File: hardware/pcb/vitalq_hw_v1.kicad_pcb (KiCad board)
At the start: 4 copper layers, 36.5 x 70 mm, 245 parts, among them J1 USB-C, J2 LiPo pads, J3 FSR pads, J5 ECG pads, J6 EDA pads, J7 Chest bioZ, J8 TC2030, Q1 CSD13380F3T, Q2 CSD13380F3T, Q3 BC847BS,115, SW1 TS-1088, SW2 TS-1088, U1 ESP32-WROOM-32E-N8R2, U10 AS7341-DLGM, U11 TMP117AIDRVR, U12 MLX90632SLD-DCB-100-SP, U13 BME280, U14 LSM6DSV80XTR, U15 TPS61240YFFR, U16 SFH 7072, U17 MAX17048G+T10, U18 W25Q512JVEIQ, U19 TCA6408ARSVR, U2 BQ25170DSGR, U20 TMP117AIDRVR, U21 USBLC6-2SC6, U3 TPS63802DLAR, U4 TPS7A2018PDBVR, U5 CP2102N-A02-GQFN28R, U6 AFE4900YZR, U7 AD5940BCBZ-RL7, U8 ADS1292RIRSMT, U9 PCA9306DCUR

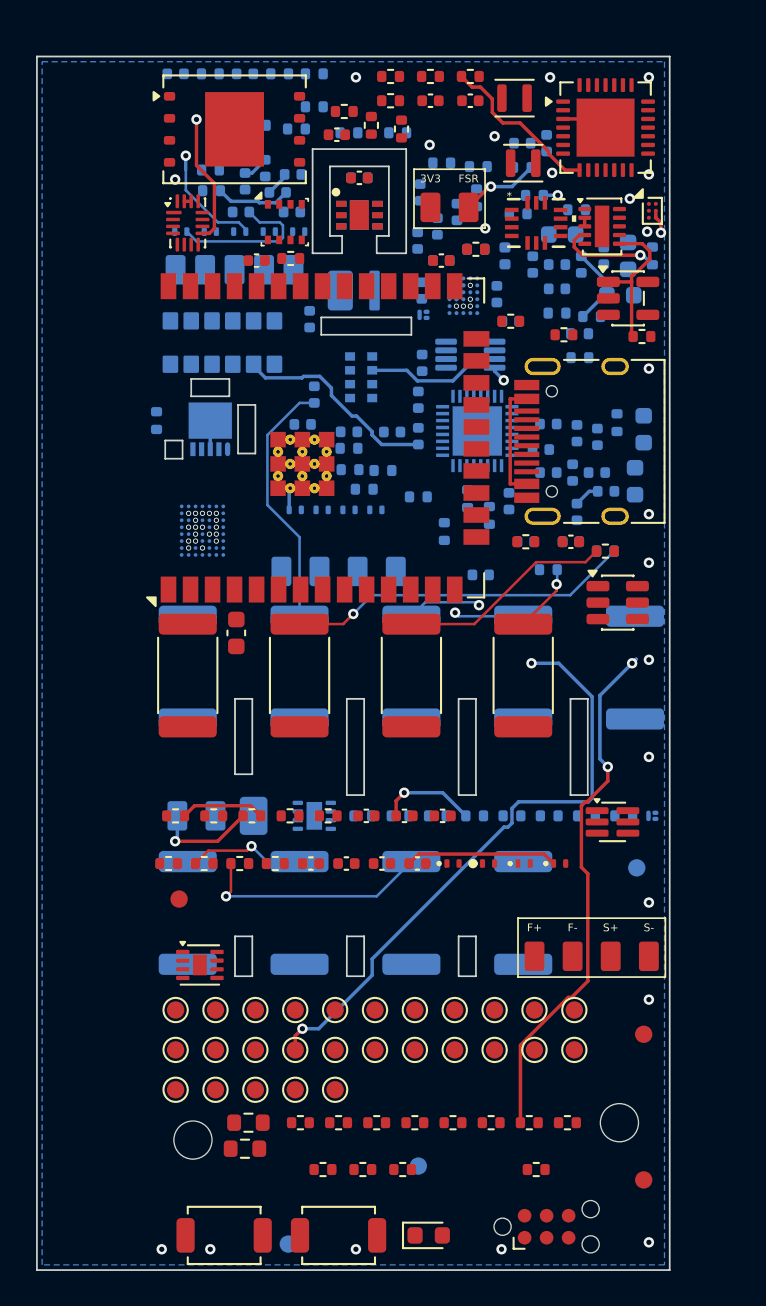
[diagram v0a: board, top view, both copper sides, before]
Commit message: Repack hw_v1 placement: skin-sensor cluster + per-IC passives, zero removals
Placement-only pass on the pcb branch — all 245 parts retained, none
removed, no footprints changed. Every skin-facing sensor stays in one
~16x16 mm bottom-side cluster around the same skin point (J5 ECG pads,
SFH7072, MLX90632, AS7341, D10+D11 LEDs, TMP117 pair). D11 (860 nm)
moved beside D10 so both emitters light the AS7341 aperture.

Per-IC support passives pulled tight: AFE4900 supply/ref network wraps
U7; ADS1292R input/RLD network hugs U8; AD5940 loop + isolated
electrode path (C54-C55, R39-R42, D6-D9) at U6 and along the J6
corridor; PCA9306 I2C pull-ups flank U9; USB-UART series resistors
moved beside the connector row.

check.sh: 0 clashes, 0 pad-to-slot/edge, 0 SMD-vs-PTH, 0 pad-miss.
Non-unconnected DRC errors 28 (vs 29 at the branch tip) — all
pre-existing (U1 pad-25 VIP vias, Q1/Q2 package proximity, J5 clamp
diodes inside the HV rule). Board remains intentionally unrouted.

Research prototype. Not a medical device.

Co-Authored-By: Devin AI <158243242+devin-ai-integration[bot]@users.noreply.github.com>
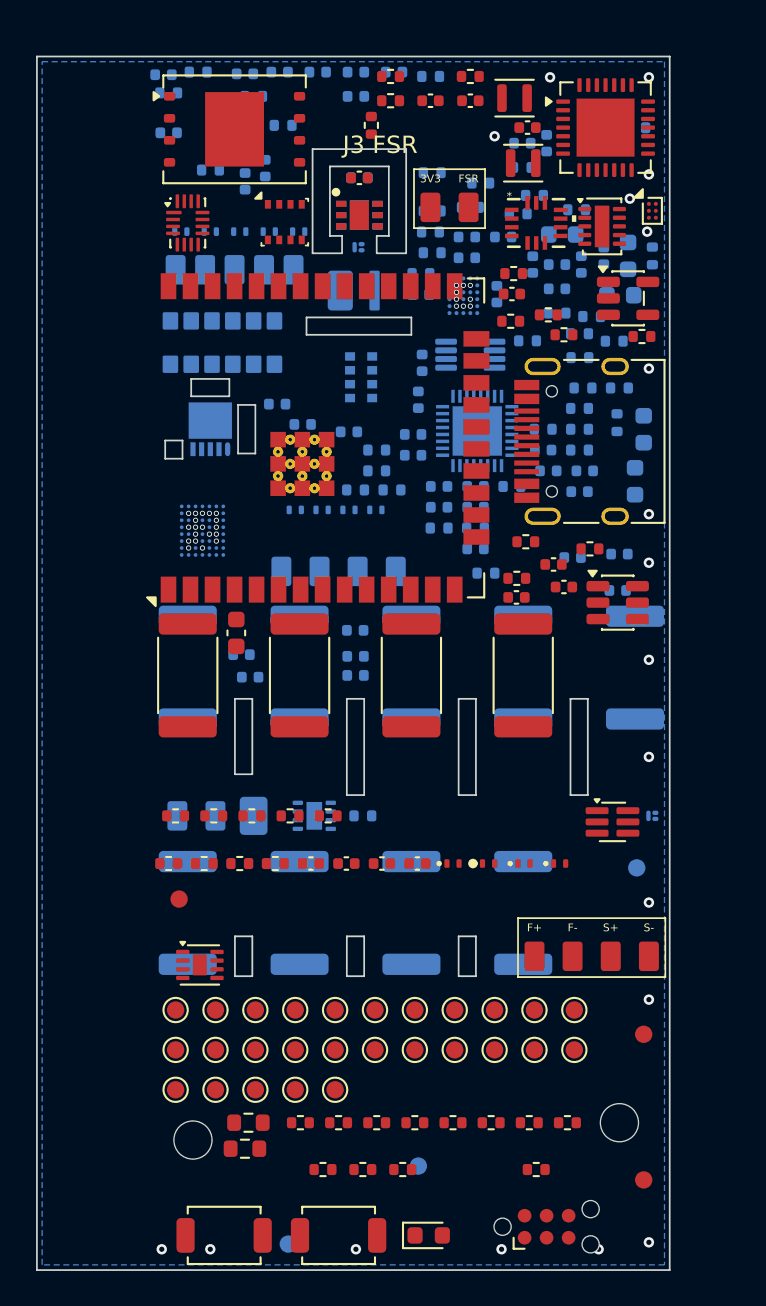
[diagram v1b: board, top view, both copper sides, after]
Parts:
- C54, C66, R53, R63: moved to B.Cu
- moved R71 41.0 mm to (32.5, 2.91)
- moved R70 40.0 mm to (32.5, 4.11)
- moved R73 39.7 mm to (34.6, 4.11)
- moved R72 38.5 mm to (32.5, 5.31)
- moved C30 32.4 mm to (25.3, 28.4)
- moved C16 31.9 mm to (7.30, 1.05)
- moved R12 30.6 mm to (7.60, 2.10), turned to 180 degrees
- moved C19 30.5 mm to (16.2, 0.90)
- moved C18 28.6 mm to (14.0, 0.90), turned to 180 degrees
- moved R18 28.1 mm to (31.5, 19.1)
- moved R30 27.9 mm to (25.9, 29.8)
- moved C24 27.6 mm to (7.60, 4.40)
- moved C26 27.1 mm to (20.6, 0.90)
- moved R13 26.3 mm to (12.5, 2.30), turned to 180 degrees
- moved C23 26.3 mm to (18.4, 0.90), turned to 180 degrees
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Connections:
- H1 pad : (no net) -> unconnected-(H1-MH-Pad1)
- H2 pad : (no net) -> unconnected-(H2-MH-Pad1)
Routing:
- net TX_5V_RAW: track 58.3 -> 0.00 mm, vias 3 -> 0
- net RLD_CLAMP: track 56.5 -> 0.00 mm, vias 3 -> 0
- net I2C_SDA_1V8: track 52.7 -> 0.00 mm, vias 3 -> 0
- net GND: track 43.9 -> 0.00 mm, vias 25 -> 26
- net AFE_P_AC: track 31.7 -> 0.00 mm, vias 3 -> 0
- net VBUS_DET: track 31.3 -> 0.00 mm, vias 2 -> 0
- net SE_SURGE: track 19.9 -> 0.00 mm, vias 1 -> 0
- net ECG_N: track 14.7 -> 0.00 mm
- net SP_SURGE: track 13.5 -> 0.00 mm, vias 1 -> 0
- net RE_SURGE: track 12.4 -> 0.00 mm
- net TX_5V: track 11.9 -> 0.00 mm
- net CP_VBUS: track 9.58 -> 0.00 mm
- net +3V3: track 9.10 -> 0.00 mm
- net ECG_P: track 8.83 -> 0.00 mm
- net SN_ISO: track 8.78 -> 0.00 mm
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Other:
- outline, holes or cut-outs redrawn
- board text added: "J3 FSR"

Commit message: Improve hw_v2 PCB: HV tail chains, decoupling re-park, power islands, U22 escape
Schematic fixes:
- Fix SWEAT_RE silently shorted to GND (D27 pin-endpoint collision)
- Fix L2/TX_5V boost miswire (VBAT_SYS->TX_SW, rail was dead)
- Add J11/J13 HV-boundary chains: R118-R122 2512 cut-points + D26-D30 DNP TPD clamps
- Correct J12 to FH12-14S-0.5SH land; R114 LED_AN fed from TX_5V
- Move U24 VBACKUP to dedicated RTC_VBK net; ADS1292 CLK grounded
- Add CS pull-ups (R115-R117), TP28, C84 (U4 +3V3 input decoupling)
- New hw_v2 parts: U22 MAX86178, U23 SHT45, U24 RTC (DNP), U25 IM69D130 (DNP),
  D12 SFH4735 NIR + Q4 gate, J9-J13 tails

Layout:
- Grow board 32->40 mm east; five 2512 HV parts could not fit at 32 mm
- Re-park ~30 decoupling passives adjacent to their ICs
- Replace phantom moat wall slots with a real >=1.0 mm channel
- Own-layer pour keepouts under HV pads; wider stitch-via HV margin
- U22 WLP: drop 28 NC lands (rows B-E) to open B.Cu escape for F-row
- Retarget dead power islands (TX_5V over its 9 loads, +1V8 under LDO, +3V3 at U7)

BOM/CPL: footprint-aware 0R mapping (0402->C17168, 2512->C2908946),
DNP parts excluded, J11/J13 pads DNP'd, U1 MPN corrected.

Gates: placement zero (291 parts), ERC 0, DRC non-unrouted 0
(9 inherent Q1/Q2/Q4 intra-package clearances waived-by-name).
Board remains unrouted by design - research prototype, not fab-ready.

Generated with [Devin](https://devin.ai)

Co-Authored-By: Devin <158243242+devin-ai-integration[bot]@users.noreply.github.com>
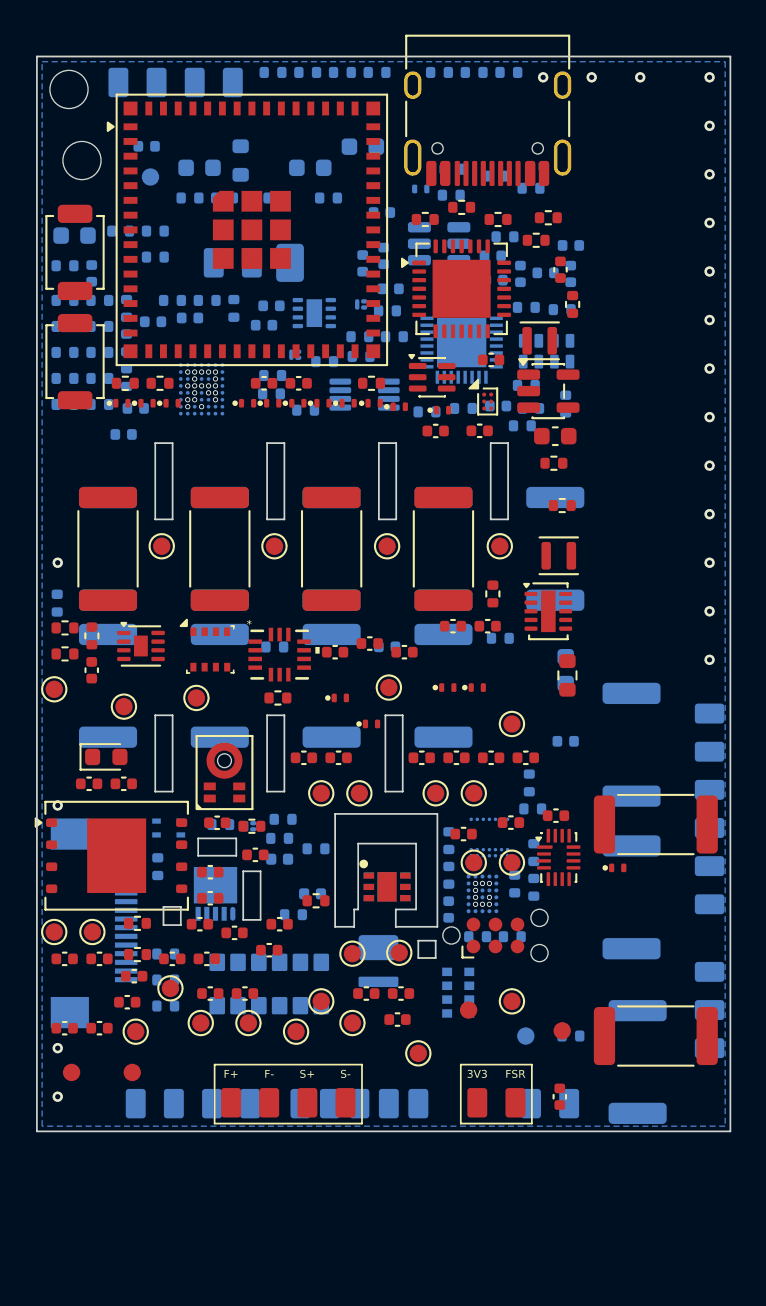
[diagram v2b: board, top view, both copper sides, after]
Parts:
- added C76: 100n, Capacitor_SMD:C_0402_1005Metric, F.Cu at (3.61, 56.0)
- added C77: 100n, Capacitor_SMD:C_0402_1005Metric, F.Cu at (19.0, 54.0)
- added C78: 100n, Capacitor_SMD:C_0402_1005Metric, F.Cu at (21.0, 54.0)
- added C79: 100n, Capacitor_SMD:C_0402_1005Metric, F.Cu at (20.8, 55.5)
- added C80: 1u, Capacitor_SMD:C_0402_1005Metric, B.Cu at (30.5, 39.5)
- added C81: 100n, Capacitor_SMD:C_0402_1005Metric, F.Cu at (30.2, 60.0)
- added C82: 1u, Capacitor_SMD:C_0402_1005Metric, F.Cu at (10.4, 44.2)
- added C83: 1u, Capacitor_SMD:C_0402_1005Metric, F.Cu at (24.6, 44.9)
- added C84: 1u, Capacitor_SMD:C_0402_1005Metric, B.Cu at (28.5, 20.3)
- added D12: SFH 4735 730nm, LED_SMD:LED_0402_1005Metric, B.Cu at (15.9, 48.3)
- added D26: TPD1E10B06, vitalq:TPD1E10B06_DPY, F.Cu at (17.5, 37.0)
- added D27: TPD1E10B06, vitalq:TPD1E10B06_DPY, F.Cu at (23.7, 36.4)
- added D28: TPD1E10B06, vitalq:TPD1E10B06_DPY, F.Cu at (25.4, 36.4)
- added D29: TPD1E10B06, vitalq:TPD1E10B06_DPY, F.Cu at (33.5, 46.8)
- added D30: TPD1E10B06, vitalq:TPD1E10B06_DPY, F.Cu at (19.3, 38.5)
- added J10: Optical tail pads, vitalq:Pads_1x06, B.Cu at (38.8, 43.4)
- added J11: Sweat site, vitalq:Pads_1x03, B.Cu at (38.8, 55.0)
- added J12: FH12-14S, Connector_FFC-FPC:Hirose_FH12-14S-0.5SH_1x14-1MP_P0.50mm_Horizontal, B.Cu at (3.30, 50.0)
- added J13: MX ECG pads, vitalq:Pads_1x02, B.Cu at (29.6, 60.4)
- added J9: I2C tail pads, vitalq:Pads_1x04, B.Cu at (8.00, 1.50)
- added Q4: CSD13380F3T, Package_DFN_QFN:Texas_PicoStar_DFN-3_0.69x0.60mm, B.Cu at (12.3, 44.4)
- added R102: 0, Resistor_SMD:R_0402_1005Metric, B.Cu at (23.9, 8.00)
- added R103: 0, Resistor_SMD:R_0402_1005Metric, B.Cu at (26.4, 6.90)
- added R104: 0, Resistor_SMD:R_0402_1005Metric, B.Cu at (28.5, 7.60)
- added R105: 0, Resistor_SMD:R_0402_1005Metric, B.Cu at (24.0, 6.50)
- added R106: 0, Resistor_SMD:R_0402_1005Metric, B.Cu at (8.83, 8.16)
- added R107: 100k, Resistor_SMD:R_0402_1005Metric, B.Cu at (10.8, 8.16)
- added R108: 100k, Resistor_SMD:R_0402_1005Metric, B.Cu at (12.8, 8.16)
- added R109: 100, Resistor_SMD:R_0402_1005Metric, F.Cu at (16.1, 48.7)
- added R110: 100k, Resistor_SMD:R_0402_1005Metric, B.Cu at (14.2, 44.0)
- added R112: 10k, Resistor_SMD:R_0402_1005Metric, B.Cu at (4.83, 10.1)
- added R113: 10k, Resistor_SMD:R_0402_1005Metric, B.Cu at (6.83, 10.1)
- added R114: 0, Resistor_SMD:R_0402_1005Metric, F.Cu at (12.4, 44.4)
- added R115: 10k, Resistor_SMD:R_0402_1005Metric, B.Cu at (28.0, 21.3)
- added R116: 10k, Resistor_SMD:R_0402_1005Metric, B.Cu at (30.8, 56.5)
- added R117: 10k, Resistor_SMD:R_0402_1005Metric, B.Cu at (28.4, 41.9)
- added R118: 0, Resistor_SMD:R_2512_6332Metric, F.Cu at (35.7, 44.3)
- added R119: 0, Resistor_SMD:R_2512_6332Metric, F.Cu at (35.7, 56.5)
- added R120: 0, Resistor_SMD:R_2512_6332Metric, B.Cu at (34.3, 48.5)
- added R121: 0, Resistor_SMD:R_2512_6332Metric, B.Cu at (34.3, 39.7)
- added R122: 0, Resistor_SMD:R_2512_6332Metric, B.Cu at (34.6, 58.0)
- added TP28: RTC_INT, TestPoint:TestPoint_Pad_D1.0mm, F.Cu at (5.02, 37.5)
- added U22: MAX86178ENJ+, vitalq:MAX86178_WLP49, B.Cu at (26.1, 45.0)
- added U23: SHT45-AD1B, vitalq:SHT45_DFN4, B.Cu at (7.60, 44.5)
- added U24: RV-3028-C7, vitalq:RV3028C7, B.Cu at (29.4, 17.0)
- added U25: IM69D130, vitalq:IM69D130, F.Cu at (10.8, 41.3)
- C13, C18, C21, C22, C26, C27, C28, C29, C3, C36, C37, C38, C39, C4, C40, C41, C46, C47, C48, C49, C50, C51, C52, C53, C54, C55, C56, C57, C58, C59, C6, C60, D1, D2, D3, D6, D7, D8, D9, FID5, H2, R39, R40, R5: moved to F.Cu
- C33, C63, C64, C68, C69, C7, R1, R100, R101, R11, R31, R41, R44, R59, R60, R61, R74, R75, R84, R85, R86, R87, R89, R90, R94, U21: moved to B.Cu
- U1: value ESP32-WROOM-32E-N8R2 -> ESP32-S3-MINI-1U-N4R2; footprint RF_Module:ESP32-WROOM-32E -> vitalq:ESP32_S3_MINI_1U
- moved H2 67.5 mm to (1.85, 1.90), turned to 0 degrees
- moved SW2 58.7 mm to (2.20, 11.3), turned to 90 degrees
- moved H1 56.9 mm to (2.60, 6.00)
- moved R94 55.5 mm to (11.8, 6.00), turned to 90 degrees
- moved J3 51.7 mm to (26.5, 60.4)
- moved SW1 51.1 mm to (2.20, 17.6), turned to 90 degrees
- moved R45 50.8 mm to (7.43, 54.8)
- moved R53 49.0 mm to (28.7, 45.9), turned to 90 degrees
- moved FID4 48.7 mm to (6.55, 6.95)
- moved J5 48.6 mm to (18.6, 60.4)
- moved R89 48.4 mm to (7.82, 14.1), turned to 180 degrees
- moved C59 48.1 mm to (7.81, 52.0), turned to 0 degrees
- moved C61 47.8 mm to (10.0, 54.0)
- moved R90 47.7 mm to (11.4, 14.5), turned to 90 degrees
- moved C60 47.2 mm to (5.61, 53.0), turned to 0 degrees
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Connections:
- L2 pad 1: TX_SW -> VBAT_SYS
- L2 pad 2: TX_5V -> TX_SW
- U1 pad 11: CS_FLASH -> CHG_PG
- U1 pad 12: CHG_PG -> I2C_SDA
- U1 pad 13: AD5940_GPIO0 -> I2C_SCL
- U1 pad 14: unconnected-(U1-IO12-Pad14) -> CS_ADS1292
- U1 pad 15: GND -> SPI_MOSI
- U1 pad 16: AFE4900_ADC_RDY -> SPI_SCK
- U1 pad 17: unconnected-(U1-NC-Pad17) -> SPI_MISO
- U1 pad 18: unconnected-(U1-NC-Pad18) -> AD5940_GPIO0
- U1 pad 19: unconnected-(U1-NC-Pad19) -> CS_AD5940
- U1 pad 2: +3V3_ESP -> GND
- U1 pad 20: unconnected-(U1-NC-Pad20) -> CS_FLASH
- U1 pad 21: unconnected-(U1-NC-Pad21) -> STATUS_LED
- U1 pad 22: unconnected-(U1-NC-Pad22) -> CS_AFE4900
- U1 pad 23: CS_AD5940 -> USB_DM_S3
- U1 pad 24: unconnected-(U1-IO2-Pad24) -> USB_DP_S3
- U1 pad 25: ESP_IO0 -> AFE4900_ADC_RDY
- U1 pad 26: CS_ADS1292 -> unconnected-(U1-IO26-Pad26)
- U1 pad 28: STATUS_LED -> unconnected-(U1-IO33-Pad28)
- U1 pad 29: CS_AFE4900 -> unconnected-(U1-IO34-Pad29)
- U1 pad 3: ESP_EN -> +3V3_ESP
- U1 pad 30: SPI_SCK -> unconnected-(U1-IO48-Pad30)
- U1 pad 31: SPI_MISO -> unconnected-(U1-IO35-Pad31)
- U1 pad 33: I2C_SDA -> unconnected-(U1-IO37-Pad33)
- U1 pad 34: ESP_RX -> CS_MAX86178
- U1 pad 35: ESP_TX -> MAX86178_INT
- U1 pad 36: I2C_SCL -> MIC_CLK
- U1 pad 37: SPI_MOSI -> MIC_DAT
- U1 pad 38: GND -> SPARE_IN
- U1 pad 39: GND -> ESP_TX
- U1 pad 4: FSR_ADC -> ESP_IO0
- U1 pad 5: unconnected-(U1-SENSOR_VN-Pad5) -> FSR_ADC
- U5 pad 4: USB_DP -> USB_DP_CP
- U5 pad 5: USB_DM -> USB_DM_CP
- U7 pad A1: unconnected-(U7-AFE4-PadA1) -> SWEAT_CE
- U7 pad A2: unconnected-(U7-AFE3-PadA2) -> SWEAT_RE
- U7 pad C5: unconnected-(U7-AIN6-PadC5) -> SWEAT_WE
- U7 pad E1: unconnected-(U7-GPIO2-PadE1) -> NIR730_GATE
- U8 pad 17: unconnected-(U8-CLK-Pad17) -> GND
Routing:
- net SWEAT_WE: vias 0 -> 1
- net GND: vias 26 -> 27
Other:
- board size 36.5 x 70 mm -> 40 x 62 mm
- board text removed: "J3 FSR"
- board text removed: "JLCJLCJLCJLC"
